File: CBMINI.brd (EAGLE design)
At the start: 100 x 60 mm, 57 parts, among them IC1 ATMEGA32U4NT, IC2 MCP2515, IC3 MCP2551, J1 USB_B_PTH, SW1 SWITCH-DPDT3, X1 INPUT, X2 OUTPUT

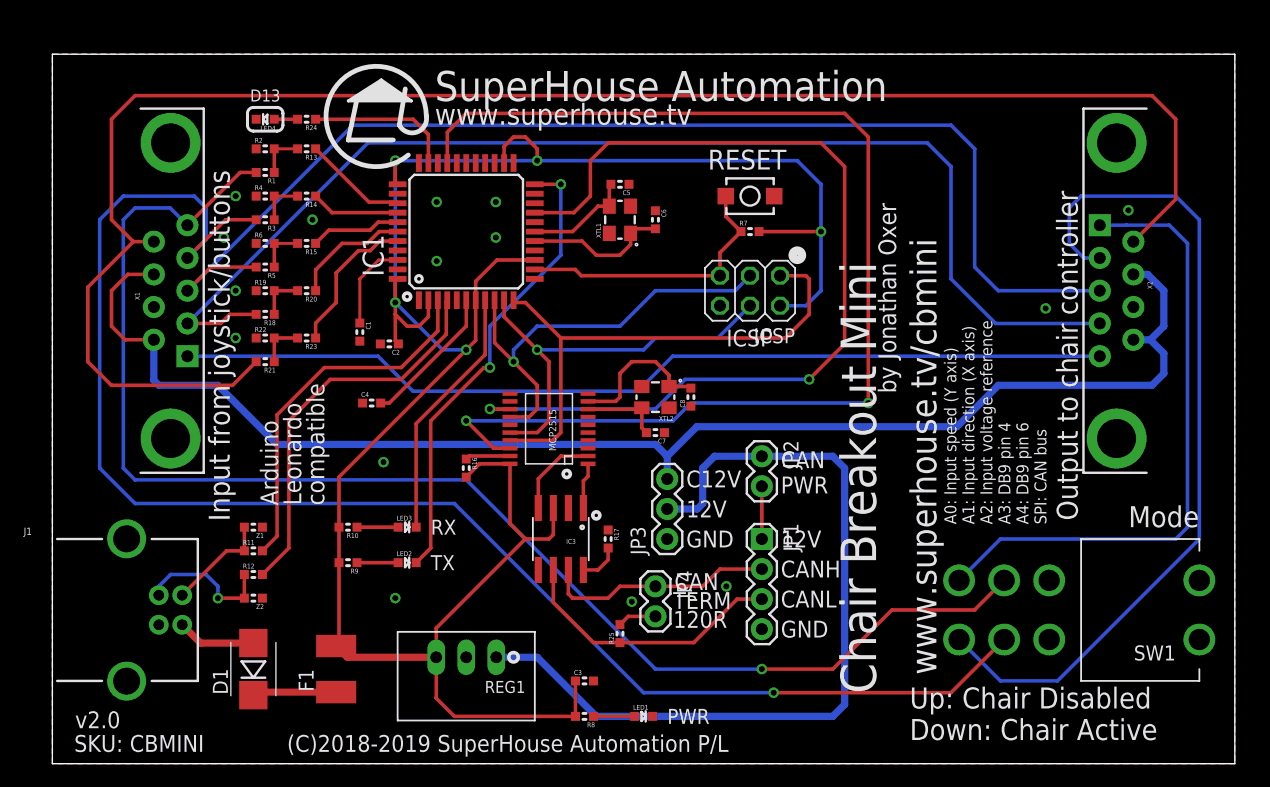
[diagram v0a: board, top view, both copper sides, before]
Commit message: Changed input 5 to pin 5 for v2.1 release
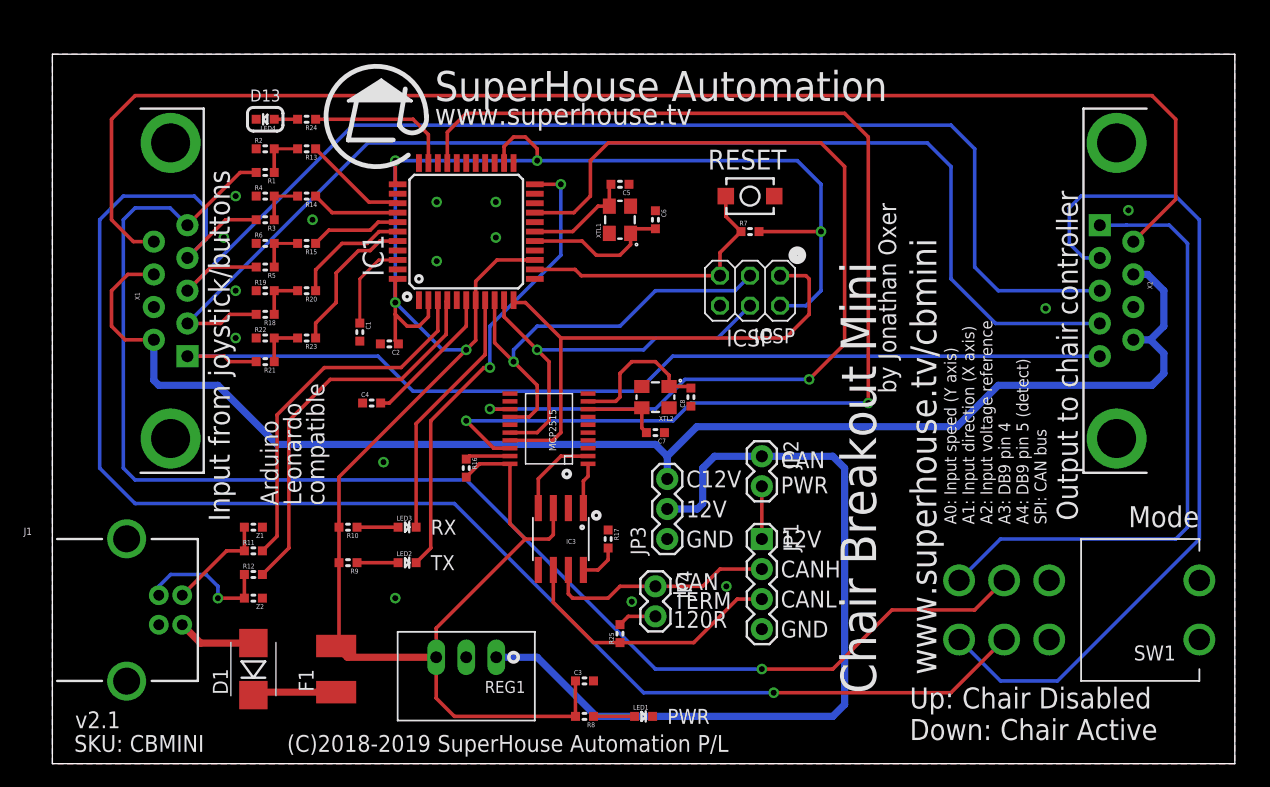
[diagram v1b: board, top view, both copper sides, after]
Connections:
- net DETECT: now also R21.2
- net PIN6: no longer R21.2
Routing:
- net PIN6: track 144.0 -> 116.3 mm
- net DETECT: track 79.6 -> 85.6 mm
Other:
- board text added: "A0: Input speed (Y axis) A1: Input direction (X axis) A2: Input voltage reference A3: DB9 pin 4 A4: DB9 pin 5 (detect) SPI: CAN bus"
- board text added: "v2.1"
- board text removed: "A0: Input speed (Y axis) A1: Input direction (X axis) A2: Input voltage reference A3: DB9 pin 4 A4: DB9 pin 6 SPI: CAN bus"
- board text removed: "v2.0"
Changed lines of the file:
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@@
 <?xml version="1.0" encoding="utf-8"?>
 <!DOCTYPE eagle SYSTEM "eagle.dtd">
-<eagle version="9.3.0">
+<eagle version="9.3.1">
 <drawing>
 <settings>
-<setting alwaysvectorfont="no"/>
+<setting alwaysvectorfont="yes"/>
 <setting keepoldvectorfont="yes"/>
 <setting verticaltext="up"/>
@@
 <grid distance="0.5" unitdist="mm" unit="mm" style="lines" multiple="1" display="yes" altdistance="0.005" altunitdist="inch" altunit="inch"/>
 <layers>
-<layer number="1" name="Top" color="4" fill="1" visible="yes" active="yes"/>
+<layer number="1" name="Top" color="12" fill="1" visible="yes" active="yes"/>
 <layer number="2" name="Route2" color="1" fill="3" visible="no" active="no"/>
 <layer number="3" name="Route3" color="4" fill="3" visible="no" active="no"/>
@@
 <layer number="14" name="Route14" color="1" fill="6" visible="no" active="no"/>
 <layer number="15" name="Route15" color="4" fill="6" visible="no" active="no"/>
-<layer number="16" name="Bottom" color="1" fill="1" visible="no" active="yes"/>
+<layer number="16" name="Bottom" color="9" fill="1" visible="yes" active="yes"/>
 <layer number="17" name="Pads" color="2" fill="1" visible="yes" active="yes"/>
 <layer number="18" name="Vias" color="2" fill="1" visible="yes" active="yes"/>
 <layer number="19" name="Unrouted" color="12" fill="1" visible="yes" active="yes"/>
 <layer number="20" name="Dimension" color="15" fill="1" visible="yes" active="yes"/>
-<layer number="21" name="tPlace" color="15" fill="1" visible="no" active="yes"/>
+<layer number="21" name="tPlace" color="15" fill="1" visible="yes" active="yes"/>
 <layer number="22" name="bPlace" color="14" fill="1" visible="no" active="yes"/>
 <layer number="23" name="tOrigins" color="15" fill="1" visible="yes" active="yes"/>
@@
 <text x="15" y="20.5" size="1.778" layer="21" font="vector" ratio="14" rot="R90">Input from joystick/buttons</text>
 <text x="91" y="20" size="1.778" layer="21" font="vector" ratio="18">Mode</text>
-<text x="1.92" y="3" size="1.4224" layer="21" font="vector" ratio="18">v2.0</text>
+<text x="1.92" y="3" size="1.4224" layer="21" font="vector" ratio="18">v2.1</text>
 <wire x1="31.626" y1="54.778" x2="30.102" y2="51.476" width="0.4064" layer="21" curve="309.2564"/>
 <wire x1="31.626" y1="54.778" x2="29.34" y2="54.016" width="0.4064" layer="21" curve="-163.361194"/>
@@
 A2: Input voltage reference
 A3: DB9 pin 4
-A4: DB9 pin 6
+A4: DB9 pin 5 (detect)
 SPI: CAN bus</text>
 <text x="72.5" y="2" size="1.778" layer="21" font="vector" ratio="18">Up: Chair Disabled
@@
 <wire x1="49.5" y1="31.5" x2="52.46" y2="34.46" width="0.3048" layer="16"/>
 <wire x1="52.46" y1="34.46" x2="88.58" y2="34.46" width="0.3048" layer="16"/>
+<contactref element="R21" pad="2"/>
+<wire x1="17.238" y1="34" x2="15" y2="34" width="0.3048" layer="1"/>
+<wire x1="15" y1="34" x2="14.54" y2="34.46" width="0.3048" layer="1"/>
+<wire x1="14.54" y1="34.46" x2="11.42" y2="34.46" width="0.3048" layer="1"/>
 </signal>
 <signal name="PIN6">
@@
 <wire x1="95" y1="54.5" x2="95" y2="47.73" width="0.3048" layer="1"/>
 <wire x1="95" y1="47.73" x2="91.42" y2="44.15" width="0.3048" layer="1"/>
-<contactref element="R21" pad="2"/>
-<wire x1="17.238" y1="34" x2="15.238" y2="32" width="0.3048" layer="1"/>
-<wire x1="15.238" y1="32" x2="5" y2="32" width="0.3048" layer="1"/>
-<wire x1="5" y1="32" x2="3" y2="34" width="0.3048" layer="1"/>
-<wire x1="3" y1="40.3" x2="6.85" y2="44.15" width="0.3048" layer="1"/>
-<wire x1="3" y1="34" x2="3" y2="40.3" width="0.3048" layer="1"/>
 </signal>
 <signal name="C12V">

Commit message: Clickety click, replace replace
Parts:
- removed S21: RESET, freetronics-jon:TACTILE_SWITCH_SMD_2PIN_TINY
- added S1: RESET, SuperHouse-Switches:TACTILE_SMT_3X4X2
- C1, C2, C3, C4, C5, C6, C7, C8: device freetronics-master-v1.1:0603 -> SuperHouse-DiscreteSemi:C0603
- D1: device freetronics-jon:SMB-DIODE -> SuperHouse-DiscreteSemi:SMA-DIODE
- F1: device rcl:L1812 -> SuperHouse-Fuses:1812
- IC1: value ATMEGA32U4NT -> ATMEGA32U4NT-TQFP; device freetronics-jon:TQFP44 -> SuperHouse-MCUs:TQFP44
- IC2: device MCP2515:TSSOP20 -> SuperHouse-ICs:TSSOP20
- IC3: device freetronics-original:SO08 -> SuperHouse-ICs:SO08
- ICSP: device pinhead:2X03 -> SuperHouse-Connectors:2X03-ICSP
- J1: value USB_B_PTH -> USB-B-PTH; device SparkFun-Connectors:USB-B-PTH -> SuperHouse-Connectors:USB-B-PTH
- JP1: device freetronics-jon:1X04 -> SuperHouse-Connectors:1X04-P
- JP2, JP4: device freetronics-jon:1X02 -> SuperHouse-Connectors:1X02-P
- JP3: device freetronics-jon:1X03 -> SuperHouse-Connectors:1X03-P
- LED1, LED2, LED3, LED4: device freetronics-jon:LED-0603 -> SuperHouse-LEDs:LED-0603
- R1, R10, R11, R12, R13, R14, R15, R18, R19, R2, R20, R21, R22, R23, R24, R3, R4, R5, R6, R8, R9: device freetronics-jon:0603 -> SuperHouse-DiscreteSemi:R0603
- R16, R17, R25, R7: device freetronics-master-v1.1:0603 -> SuperHouse-DiscreteSemi:R0603
- REG1: device freetronics-jon:K78XX-500R3 -> SuperHouse-Regulators:K78XX-500R3
- XTL1, XTL2: device freetronics-jon:CRYSTAL-SMD-3X2 -> SuperHouse-Oscillators:CRYSTAL-SMD-3X2
- Z1, Z2: device freetronics-master-v1.1:0603 -> SuperHouse-DiscreteSemi:TVS0603
- turned D1 to 270 degrees
- renumbered SW1 to S2
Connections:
- net GND: now also S1.1; no longer S21.1
- net RESET: now also S1.2; no longer S21.2
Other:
- board text added: "Up: Stop Chair Down: Move Chair"
- board text removed: "Up: Chair Disabled Down: Chair Active"

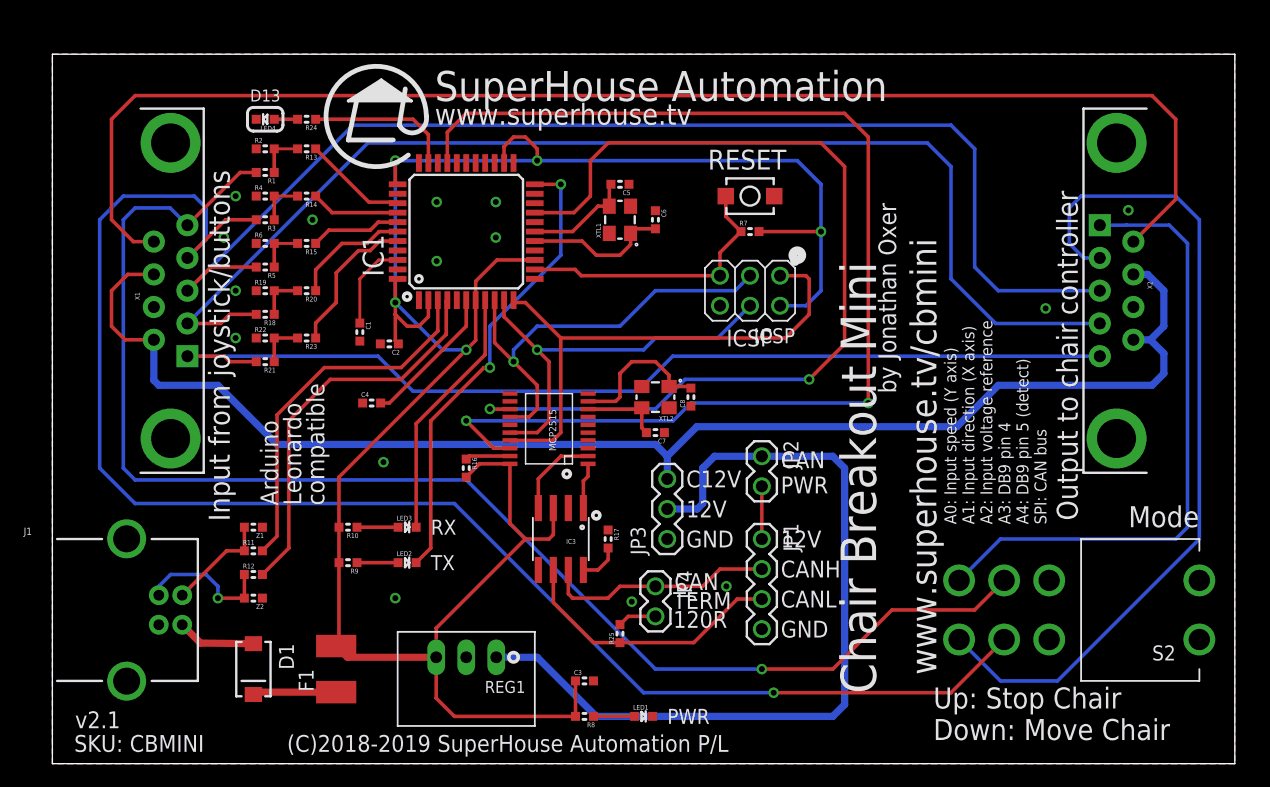
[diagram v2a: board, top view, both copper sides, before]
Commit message: Restructured voltage regulators to support 24V CAN or Permobil controller for v2.2 release
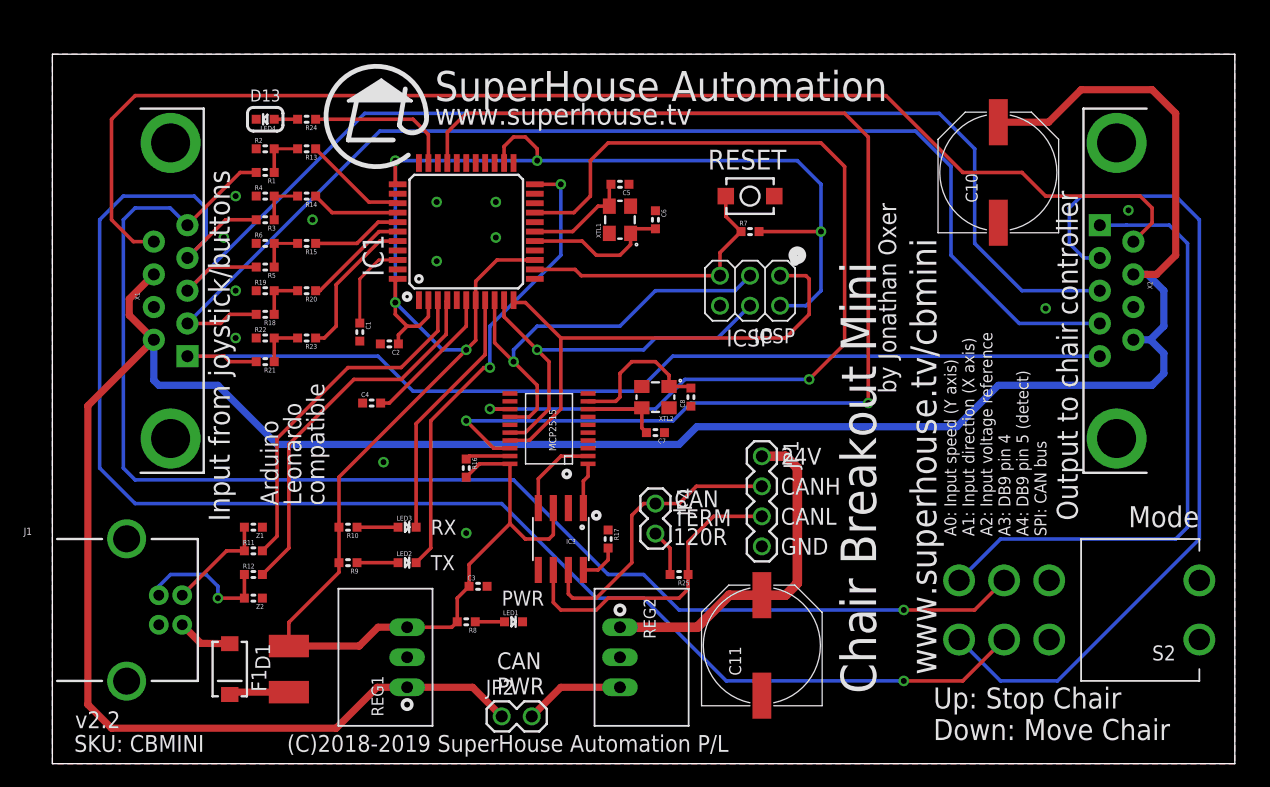
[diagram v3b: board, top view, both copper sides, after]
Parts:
- removed JP3: PWR, SuperHouse-Connectors:1X03-P
- added C10, C11: 220uF 50V, SuperHouse-DiscreteSemi:PANASONIC_G
- added REG2: K7812-500R3, SuperHouse-Regulators:K78XX-500R3
- JP4: value PWR -> CAN TERM
- moved JP2 31.1 mm to (38.0, 4.00), turned to 0 degrees
- moved LED1 13.6 mm to (39.0, 12.0)
- moved R8 12.8 mm to (35.0, 12.0)
- moved C3 12.0 mm to (36.0, 15.0)
- moved R25 7.07 mm to (53.0, 16.0), turned to 180 degrees
- moved JP1 7.00 mm to (60.0, 26.0)
- moved JP4 7.00 mm to (51.0, 22.0)
- moved REG1 5.00 mm to (30.0, 9.00), turned to 90 degrees
- moved F1 4.00 mm to (20.0, 8.00)
- moved D1 2.00 mm to (15.0, 8.00)
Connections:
- removed net C12V: JP3.3, X1.7, X1.9, X2.7, X2.9
- removed net N$15: JP1.1, JP2.2
- new net 24V: C11.+, JP1.1, REG2.1
- new net VREF: C10.+, JP2.1, REG1.1, X1.7, X1.9, X2.7, X2.9
- net 12V: now also JP2.2, REG2.3; no longer JP2.1, JP3.2, REG1.1
- net GND: now also C10.-, C11.-, REG2.2; no longer JP3.1
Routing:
- net VREF: track 0.00 -> 218.0 mm
- net C12V: track 120.1 -> 0.00 mm
- net 12V: track 71.0 -> 8.48 mm
- net 24V: track 0.00 -> 29.7 mm
- net 5V: track 191.5 -> 176.8 mm
- net PIN6: track 116.3 -> 109.1 mm
- net CANH: track 19.6 -> 24.8 mm
- net N$15: track 4.46 -> 0.00 mm
- net SPEED_IN: track 119.7 -> 115.6 mm
- net CANL: track 23.3 -> 26.3 mm
- net N$17: track 7.07 -> 5.07 mm
- net USB+: track 6.66 -> 4.67 mm
- net RD-: track 31.2 -> 30.0 mm
- net RD+: track 33.2 -> 32.0 mm
- net MISO: track 45.3 -> 44.1 mm
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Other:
- board text added: "24V"
- board text added: "v2.2"
- board text removed: "12V"
- board text removed: "C12V"
- board text removed: "v2.1"
